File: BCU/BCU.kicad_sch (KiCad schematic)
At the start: 5 parts, among them J1 USB_C_Receptacle_USB2.0

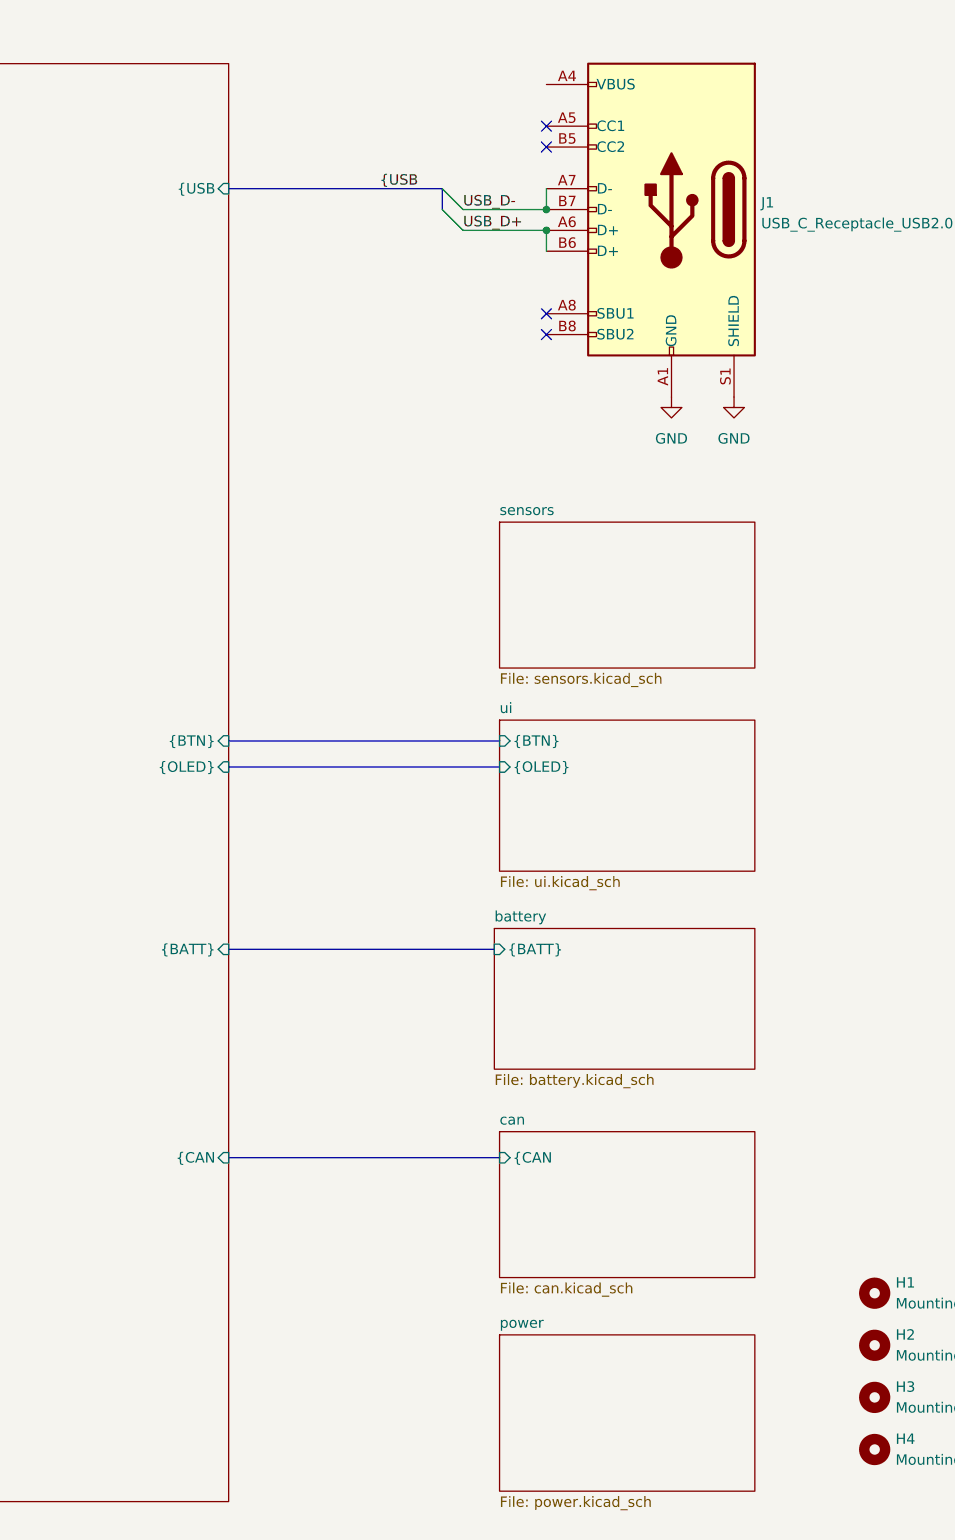
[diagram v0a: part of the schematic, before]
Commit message: Added power enable logic
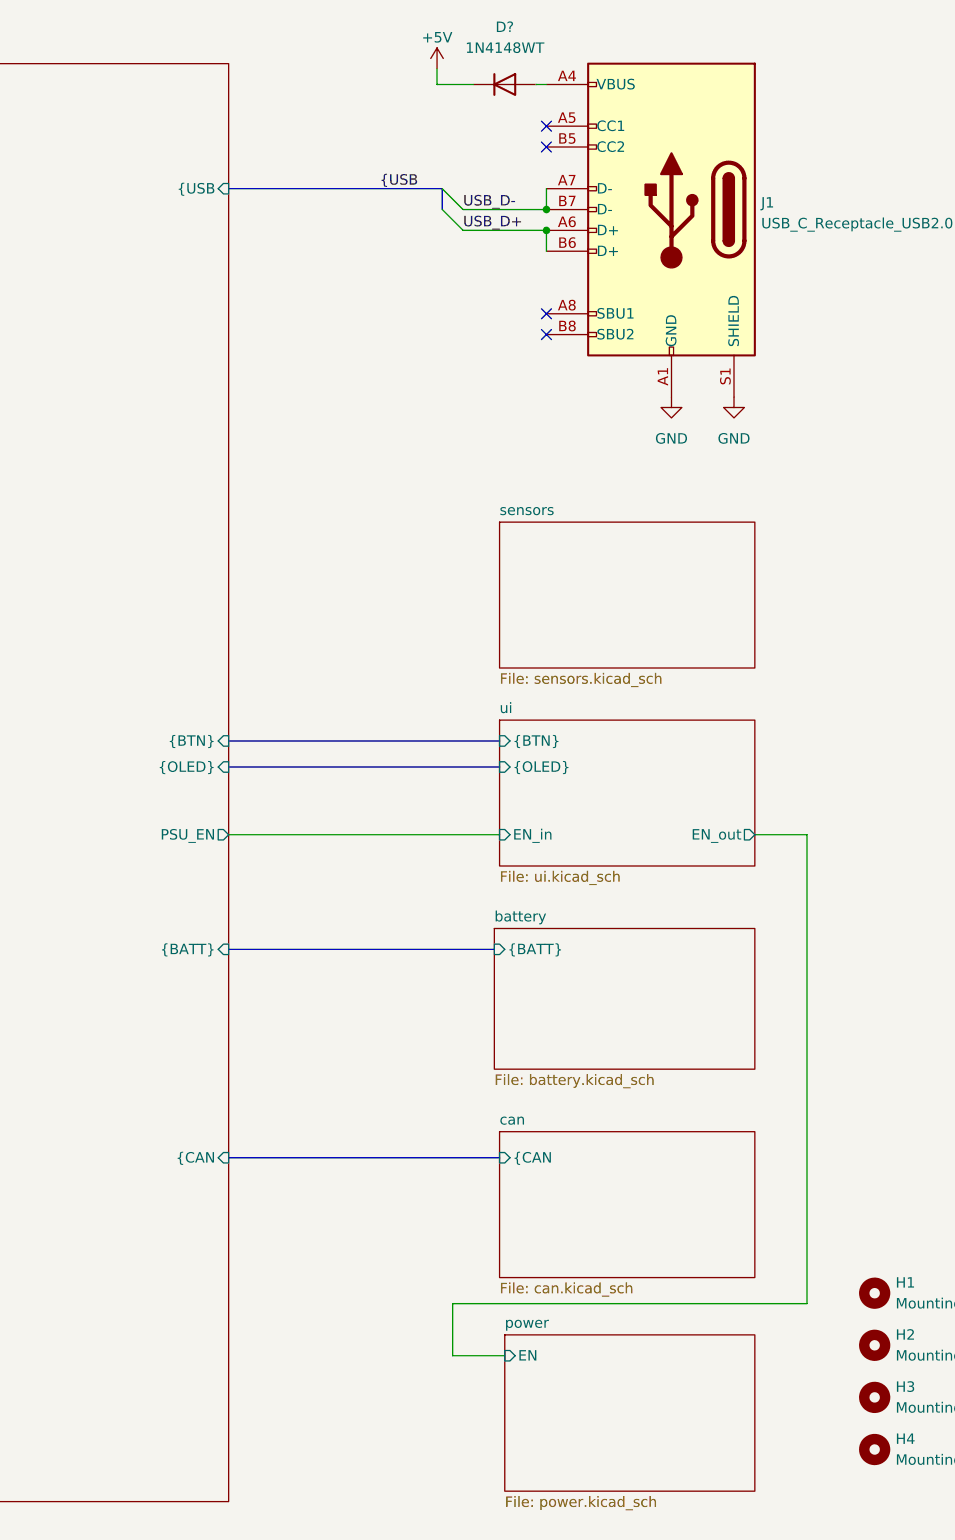
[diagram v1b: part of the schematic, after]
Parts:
- added D?: 1N4148WT, Diode_SMD:D_SOD-523, symbol Diode:1N4148WT
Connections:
- net at J1.A4 (VBUS), J1.A9 (VBUS), J1.B4 (VBUS)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: now also D?.2 (A)
- new net +5V: D?.1 (K)
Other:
- sheet mcu ports: added PSU_EN; removed none
- sheet power ports: added EN; removed none
- sheet ui ports: added EN_in, EN_out; removed none
